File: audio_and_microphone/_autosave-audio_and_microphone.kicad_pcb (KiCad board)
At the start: 2 copper layers, 81.7 x 60.4 mm, 23 parts, among them J10 Conn_01x02_Pin, J4 Conn_01x03_Pin, J5 Conn_01x02, J7 Conn_01x02

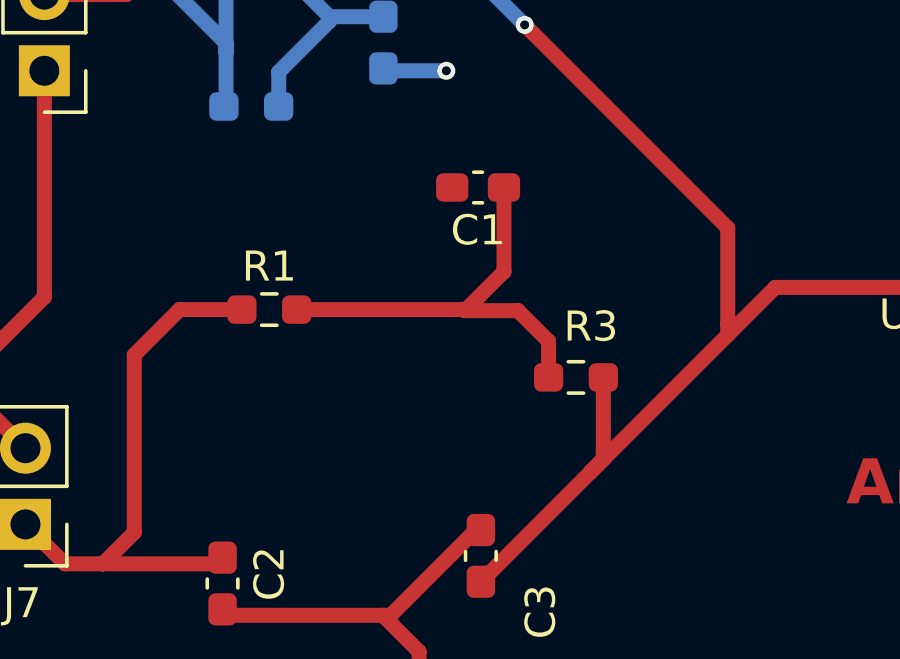
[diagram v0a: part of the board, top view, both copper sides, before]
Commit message: updated track properties, deleted switch, and fixed design rules errors
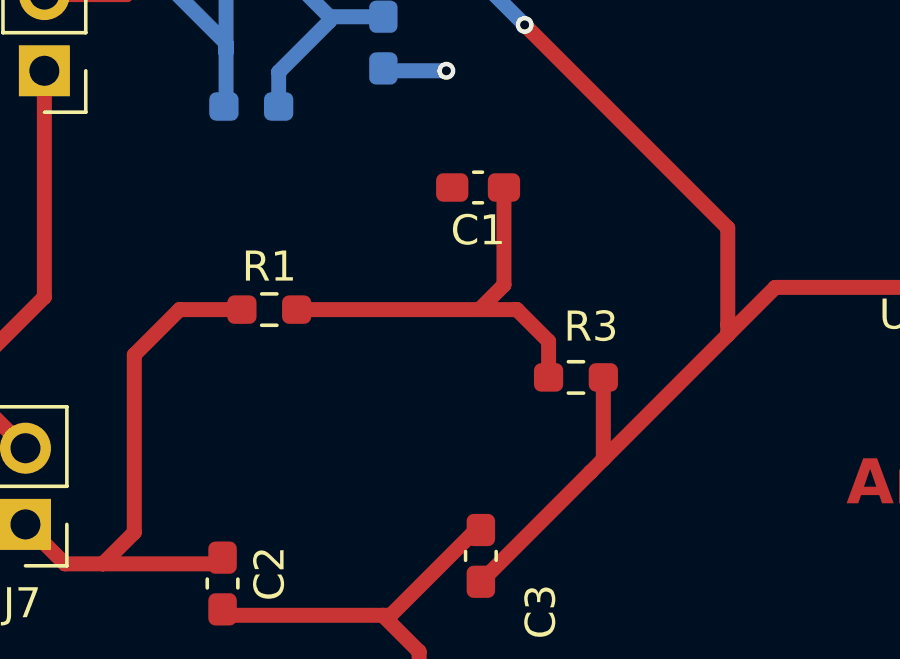
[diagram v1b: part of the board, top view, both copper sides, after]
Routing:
- net /after new filter: track 64.1 -> 63.2 mm
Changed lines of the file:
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@@
 	)
 	(segment
-		(start 129.905 101.06)
-		(end 129.94 101.095)
-		(width 0.5)
-		(layer "F.Cu")
-		(net 1)
-	)
-	(segment
-		(start 129.94 101.095)
-		(end 131.24 99.795)
+		(start 131.24 96.99)
+		(end 131.24 100.24)
+		(width 0.5)
+		(layer "F.Cu")
+		(net 1)
+	)
+	(segment
+		(start 131.24 100.24)
+		(end 130.42 101.06)
 		(width 0.5)
 		(layer "F.Cu")
@@
 	)
 	(segment
-		(start 131.7075 101.095)
+		(start 131.6725 101.06)
 		(end 132.7275 102.115)
 		(width 0.5)
@@
 	)
 	(segment
-		(start 131.24 99.795)
-		(end 131.24 96.99)
-		(width 0.5)
-		(layer "F.Cu")
-		(net 1)
-	)
-	(segment
 		(start 124.33 101.06)
-		(end 129.905 101.06)
-		(width 0.5)
-		(layer "F.Cu")
-		(net 1)
-	)
-	(segment
-		(start 129.94 101.095)
-		(end 131.7075 101.095)
+		(end 130.42 101.06)
+		(width 0.5)
+		(layer "F.Cu")
+		(net 1)
+	)
+	(segment
+		(start 130.42 101.06)
+		(end 131.6725 101.06)
 		(width 0.5)
 		(layer "F.Cu")
@@
 	)
 	(segment
-		(start 134.5525 106.05)
-		(end 134.13125 106.47125)
-		(width 0.5)
-		(layer "F.Cu")
-		(net 38)
-	)
-	(segment
 		(start 138.7 101.56)
 		(end 138.7 101.9025)
@@
 		(width 0.5)
 		(layer "F.Cu")
-		(net 38)
-	)
-	(segment
-		(start 134.5525 106.05)
-		(end 134.5525 105.7075)
-		(width 0.5)
-		(layer "F.Cu")
